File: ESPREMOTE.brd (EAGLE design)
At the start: 47 x 78 mm, 38 parts, among them IC1 ESP12SMT, IC3 LD111733, P1 USB-6PSMT, Q1 2N7002, Q2 2N7002, Q3 2N7002, Q4 2N7002

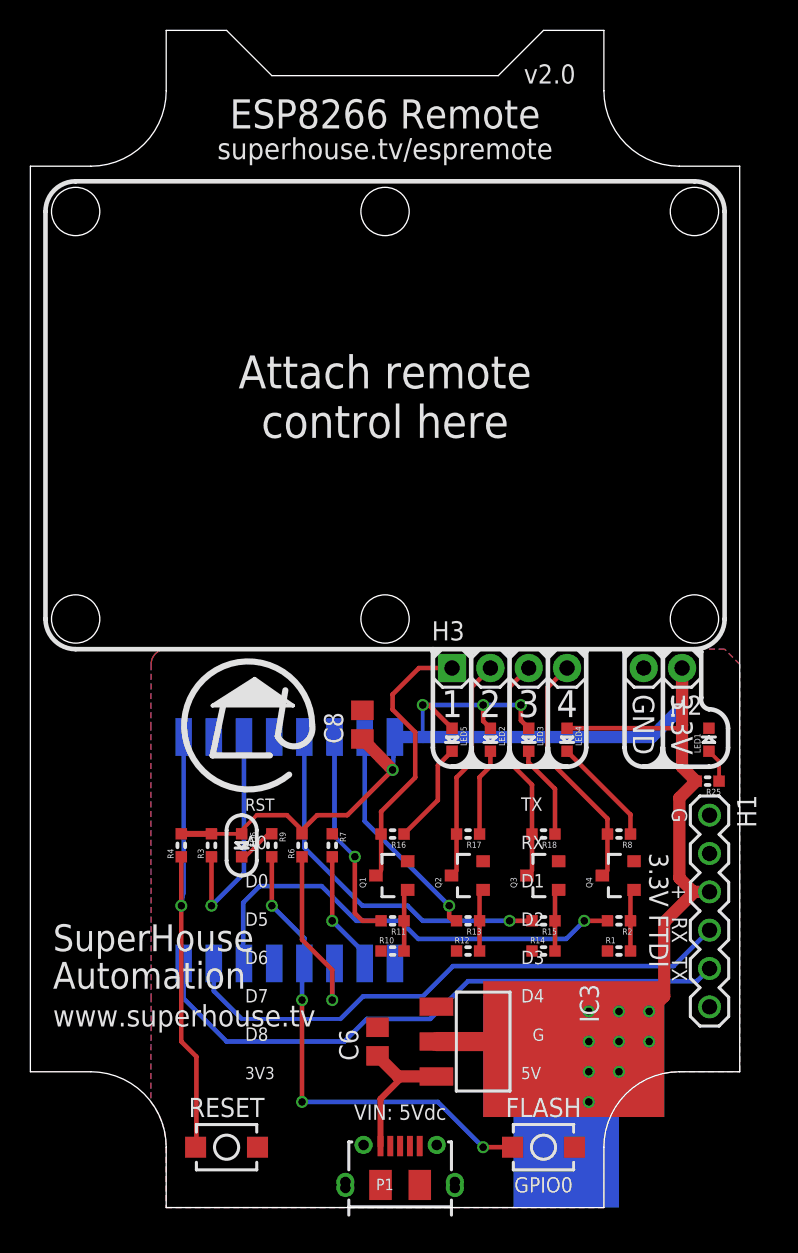
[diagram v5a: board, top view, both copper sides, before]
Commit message: Replaced crappy SMPS with linear reg and micro USB socket
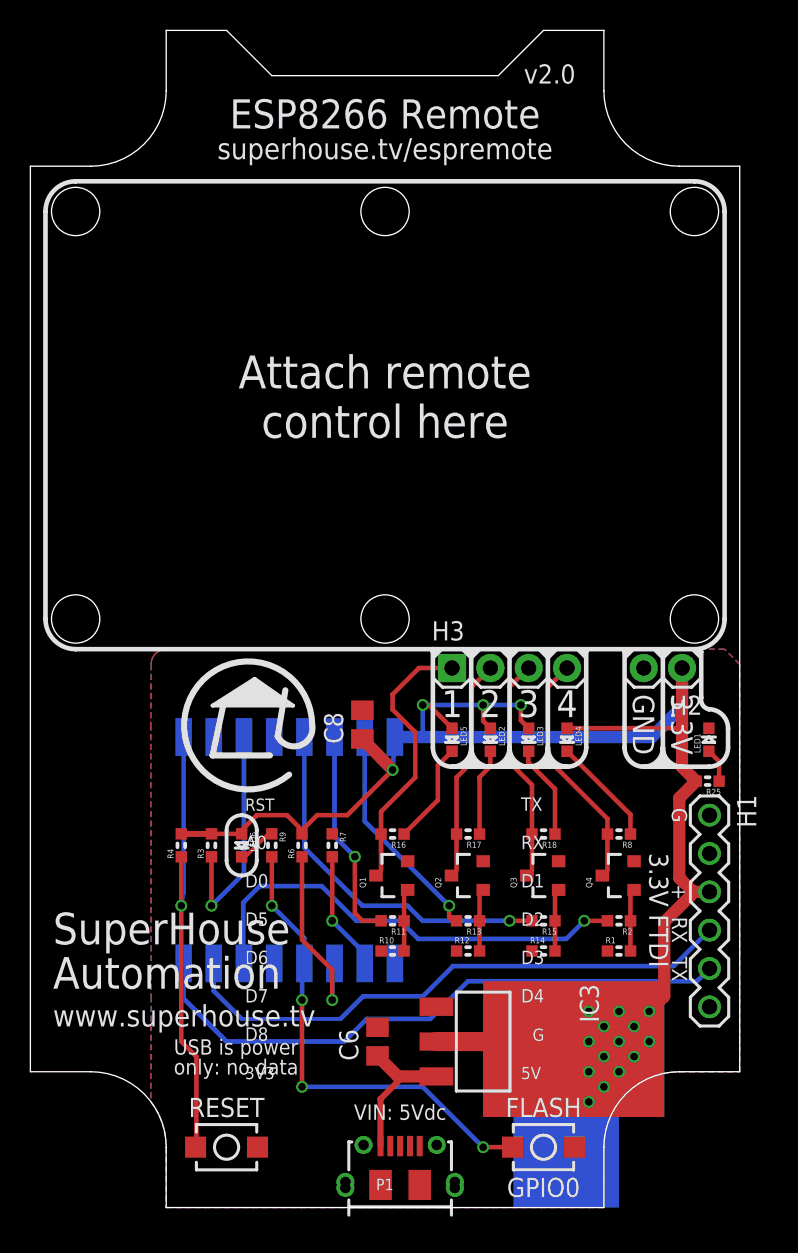
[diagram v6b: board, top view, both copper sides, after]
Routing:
- net 3.3V: track 122.3 -> 130.0 mm, vias 13 -> 18
- net GPIO0: track 32.4 -> 31.8 mm
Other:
- board text added: "USB is power only: no data"
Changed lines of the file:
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@@
 <?xml version="1.0" encoding="utf-8"?>
 <!DOCTYPE eagle SYSTEM "eagle.dtd">
-<eagle version="6.5.0">
+<eagle version="8.3.0">
 <drawing>
 <settings>
 <setting alwaysvectorfont="no"/>
+<setting keepoldvectorfont="yes"/>
 <setting verticaltext="up"/>
 </settings>
@@
 <hole x="44" y="66" drill="3.2"/>
 <hole x="3" y="66" drill="3.2"/>
-<text x="24.5" y="5.814" size="1.016" layer="21" font="vector" ratio="13" rot="SR0" align="bottom-center">VIN: 5Vdc</text>
+<text x="24.5" y="5.814" size="1.016" layer="21" font="vector" ratio="18" rot="SR0" align="bottom-center">VIN: 5Vdc</text>
 <text x="13" y="6" size="1.27" layer="21" font="vector" ratio="18" distance="40" rot="SR0" align="bottom-center">RESET</text>
 <text x="40.186" y="59.158" size="1.7" layer="22" font="vector" ratio="15" rot="MR0">Arduino board profile:
@@
 <wire x1="46.228" y1="31.75" x2="44.958" y2="33.02" width="0.3048" layer="21" curve="90"/>
 <wire x1="44.958" y1="33.02" x2="44.45" y2="33.782" width="0.3048" layer="21" curve="-90"/>
-<text x="34" y="1" size="1.016" layer="21" font="vector" ratio="18" distance="40" rot="SR0" align="bottom-center">GPIO0</text>
+<text x="34" y="0.7" size="1.27" layer="21" font="vector" ratio="18" distance="40" rot="SR0" align="bottom-center">GPIO0</text>
 <text x="41" y="19.7" size="1.27" layer="21" font="vector" ratio="18" distance="40" rot="SR270" align="bottom-center">3.3V FTDI</text>
 <text x="42.5" y="26" size="1.016" layer="21" font="vector" ratio="18" distance="40" rot="SR270" align="bottom-center">G</text>
@@
 <text x="42.5" y="15.8" size="1.016" layer="21" font="vector" ratio="18" distance="40" rot="SR270" align="bottom-center">TX</text>
 <text x="42.5" y="18.4" size="1.016" layer="21" font="vector" ratio="18" distance="40" rot="SR270" align="bottom-center">RX</text>
-<text x="1.5" y="14.5" size="1.778" layer="21" font="vector" ratio="18" distance="40" rot="SR0">SuperHouse
+<text x="1.5" y="14.5" size="2.1" layer="21" font="vector" ratio="18" distance="40" rot="SR0">SuperHouse
 Automation</text>
 <text x="1.5" y="12" size="1.4224" layer="21" font="vector" ratio="15">www.superhouse.tv</text>
@@
 <rectangle x1="30" y1="6" x2="42" y2="14" layer="16"/>
 <rectangle x1="32" y1="0" x2="39" y2="7" layer="16"/>
+<text x="9.5" y="8.814" size="1.016" layer="21" font="vector" ratio="18" distance="30" rot="SR0">USB is power
+only: no data</text>
 </plain>
 <attributes>
@@
 <pass name="Default">
 <param name="RoutingGrid" value="50mil"/>
+<param name="AutoGrid" value="1"/>
+<param name="Efforts" value="0"/>
+<param name="TopRouterVariant" value="1"/>
 <param name="tpViaShape" value="round"/>
 <param name="PrefDir.1" value="|"/>
@@
 <wire x1="22" y1="19" x2="21.5" y2="19.5" width="0.3048" layer="1"/>
 <wire x1="21.5" y1="19.5" x2="21.5" y2="23.25" width="0.3048" layer="1"/>
-<wire x1="21.5" y1="23.25" x2="20.154" y2="24.596" width="0.254" layer="16"/>
+<wire x1="21.5" y1="23.25" x2="20.154" y2="24.596" width="0.3048" layer="16"/>
 <wire x1="20.154" y1="24.596" x2="20.154" y2="31.178" width="0.3048" layer="16"/>
 </signal>
@@
 <contactref element="S2" pad="2"/>
 <via x="16" y="20" extent="1-16" drill="0.5"/>
-<wire x1="18" y1="7" x2="18" y2="13.75" width="0.3048" layer="1"/>
+<wire x1="18" y1="8" x2="18" y2="13.75" width="0.3048" layer="1"/>
 <via x="18" y="13.75" extent="1-16" drill="0.5"/>
 <contactref element="R9" pad="2"/>
@@
 <wire x1="31.95" y1="4" x2="30" y2="4" width="0.3048" layer="1"/>
 <via x="30" y="4" extent="1-16" drill="0.5"/>
-<wire x1="30" y1="4" x2="27" y2="7" width="0.3048" layer="16"/>
-<wire x1="27" y1="7" x2="18" y2="7" width="0.3048" layer="16"/>
-<via x="18" y="7" extent="1-16" drill="0.5"/>
+<wire x1="30" y1="4" x2="26" y2="8" width="0.3048" layer="16"/>
+<wire x1="26" y1="8" x2="18" y2="8" width="0.3048" layer="16"/>
+<via x="18" y="8" extent="1-16" drill="0.5"/>
 </signal>
 <signal name="GPIO2">
@@
 <wire x1="43.18" y1="29.186" x2="44.11" y2="28.256" width="0.8128" layer="1"/>
 <contactref element="LED6" pad="A"/>
-<wire x1="12" y1="24.762" x2="14" y2="24.762" width="0.254" layer="1"/>
+<wire x1="12" y1="24.762" x2="14" y2="24.762" width="0.3048" layer="1"/>
 <wire x1="14" y1="24.762" x2="14" y2="25" width="0.254" layer="1"/>
-<wire x1="14" y1="25" x2="15" y2="26" width="0.254" layer="1"/>
+<wire x1="14" y1="25" x2="15" y2="26" width="0.3048" layer="1"/>
 <wire x1="15" y1="26" x2="17" y2="26" width="0.3048" layer="1"/>
 <wire x1="17" y1="26" x2="18" y2="25" width="0.3048" layer="1"/>
@@
 <wire x1="24.154" y1="31.178" x2="26" y2="31.178" width="0.8128" layer="16"/>
 <wire x1="43.18" y1="35.75" x2="43.18" y2="33.18" width="0.8128" layer="16"/>
-<wire x1="43.18" y1="33.18" x2="42" y2="32" width="0.8128" layer="16"/>
+<wire x1="43.18" y1="33.18" x2="41.178" y2="31.178" width="0.8128" layer="16"/>
 <via x="26" y="33.3" extent="1-16" drill="0.5"/>
-<wire x1="42" y1="32" x2="41.8" y2="31.8" width="0.8128" layer="16"/>
-<wire x1="26" y1="33.3" x2="26" y2="31.178" width="0.254" layer="16"/>
+<wire x1="26" y1="33.3" x2="26" y2="31.178" width="0.3048" layer="16"/>
 <wire x1="30.48" y1="31.762" x2="30" y2="32.242" width="0.3048" layer="1"/>
 <wire x1="30" y1="32.242" x2="30" y2="33.3" width="0.3048" layer="1"/>
@@
 <wire x1="41" y1="11" x2="41" y2="13" width="0.8128" layer="16"/>
 <wire x1="26" y1="31.178" x2="41.178" y2="31.178" width="0.8128" layer="16"/>
-<wire x1="41.178" y1="31.178" x2="41.8" y2="31.8" width="0.8128" layer="16"/>
+<via x="40" y="12" extent="1-16" drill="0.5"/>
+<via x="38" y="12" extent="1-16" drill="0.5"/>
+<via x="38" y="10" extent="1-16" drill="0.5"/>
+<via x="40" y="10" extent="1-16" drill="0.5"/>
+<via x="38" y="8" extent="1-16" drill="0.5"/>
+<wire x1="38" y1="8" x2="38" y2="10" width="0.4064" layer="16"/>
+<wire x1="39" y1="9" x2="40" y2="10" width="0.4064" layer="16"/>
+<wire x1="37" y1="11" x2="38" y2="12" width="0.4064" layer="16"/>
+<wire x1="41" y1="11" x2="40" y2="12" width="0.4064" layer="16"/>
+<wire x1="39" y1="9" x2="38" y2="8" width="0.4064" layer="16"/>
 </signal>
 <signal name="N$23">
 <contactref element="LED1" pad="A"/>
 <contactref element="R25" pad="1"/>
-<wire x1="45.634" y1="28.256" x2="45.634" y2="29.562" width="0.254" layer="1"/>
-<wire x1="45.634" y1="29.562" x2="44.958" y2="30.238" width="0.254" layer="1"/>
+<wire x1="45.634" y1="28.256" x2="45.634" y2="29.562" width="0.3048" layer="1"/>
+<wire x1="45.634" y1="29.562" x2="44.958" y2="30.238" width="0.3048" layer="1"/>
 </signal>
 <signal name="CH_PD">

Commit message: Replaced USB socket and linear reg with 2.1mm DC jack and SMPS module
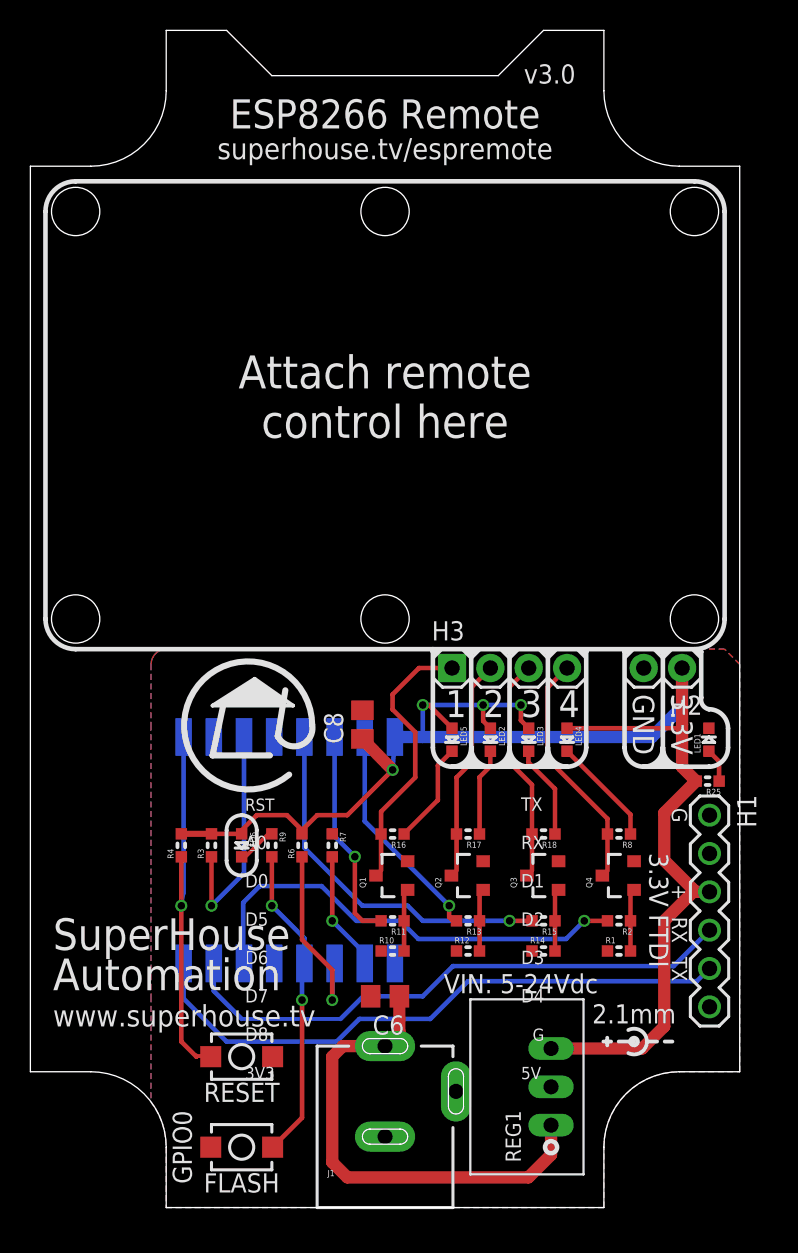
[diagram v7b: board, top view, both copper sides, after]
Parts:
- removed IC3: LD111733, freetronics-luke:SOT-223
- removed P1: USB-6PSMT, freetronics-jon:USB-MICROB-MB05PMXX
- added J1: 2.1MM DC Jack, freetronics-jon:POWER_JACK_PTH_SLOTS
- added REG1: K7803-500R3, freetronics-jon:K78XX-500R3
- moved S2 20.0 mm to (14.0, 4.00), turned to 0 degrees
- moved S1 6.08 mm to (14.0, 10.0)
- moved C6 3.04 mm to (23.5, 14.0), turned to 180 degrees
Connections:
- net 3.3V: now also REG1.3; no longer IC3.2, IC3.4
- net 5V: now also J1.PWR, REG1.1; no longer IC3.3, P1.VBUS
- net GND: now also J1.GND, J1.GNDBREAK, REG1.2; no longer IC3.1, P1.FIX1, P1.FIX2, P1.GND, P1.PIN1, P1.PIN2, P1.TAB1, P1.TAB2
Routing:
- net 3.3V: track 130.0 -> 102.9 mm, vias 18 -> 4
- net 5V: track 9.94 -> 32.0 mm
- net GPIO0: track 31.8 -> 21.0 mm, vias 4 -> 2
- net RST: track 30.9 -> 25.8 mm
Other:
- board text added: "2.1mm"
- board text added: "VIN: 5-24Vdc"
- board text added: "v3.0"
- board text removed: "USB is power only: no data"
- board text removed: "VIN: 5Vdc"
- board text removed: "v2.0"
